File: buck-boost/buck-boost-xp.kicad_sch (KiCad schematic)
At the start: 0 parts

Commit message: Working on power stage of buck-boost plat
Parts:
- added C10, C11, C8, C9: TBD, Capacitor_THT:CP_Radial_D18.0mm_P7.50mm, symbol Device:C_Polarized
- added HS1: Q1, Heatsink:Heatsink_Stonecold_HS-132_32x14mm_2xFixation1.5mm, symbol Mechanical:Heatsink_Pad_2Pin
- added HS2: Q2, Heatsink:Heatsink_Stonecold_HS-132_32x14mm_2xFixation1.5mm, symbol Mechanical:Heatsink_Pad_2Pin
- added HS3: Q3, Heatsink:Heatsink_Stonecold_HS-132_32x14mm_2xFixation1.5mm, symbol Mechanical:Heatsink_Pad_2Pin
- added HS4: Q4, Heatsink:Heatsink_Stonecold_HS-132_32x14mm_2xFixation1.5mm, symbol Mechanical:Heatsink_Pad_2Pin
- added K1, K2: Relay_SPDT, symbol Relay:Relay_SPDT
- added L1: L_Small, symbol Device:L_Small
- added Q1, Q2, Q3, Q4: Q_NMOS_GDS, Package_TO_SOT_THT:TO-220-3_Vertical, symbol Device:Q_NMOS_GDS
- added R6: R_Small, symbol Device:R_Small
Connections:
- new net: L1.1, Q1.3 (S), Q2.2 (D)
- new net: K1.11, R6.1
- new net: C8.1, C9.1, K1.14, Q1.2 (D), R6.2
- new net: C10.1, C11.1, K2.14, Q3.2 (D)
- new net: C10.2, C11.2, Q4.3 (S)
- new net: C8.2, C9.2, Q2.3 (S)
- new net IL+: L1.2
- new net IL-: Q3.3 (S), Q4.2 (D)
- no-connect marks 0 -> 8
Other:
- note added: "Snubber?"

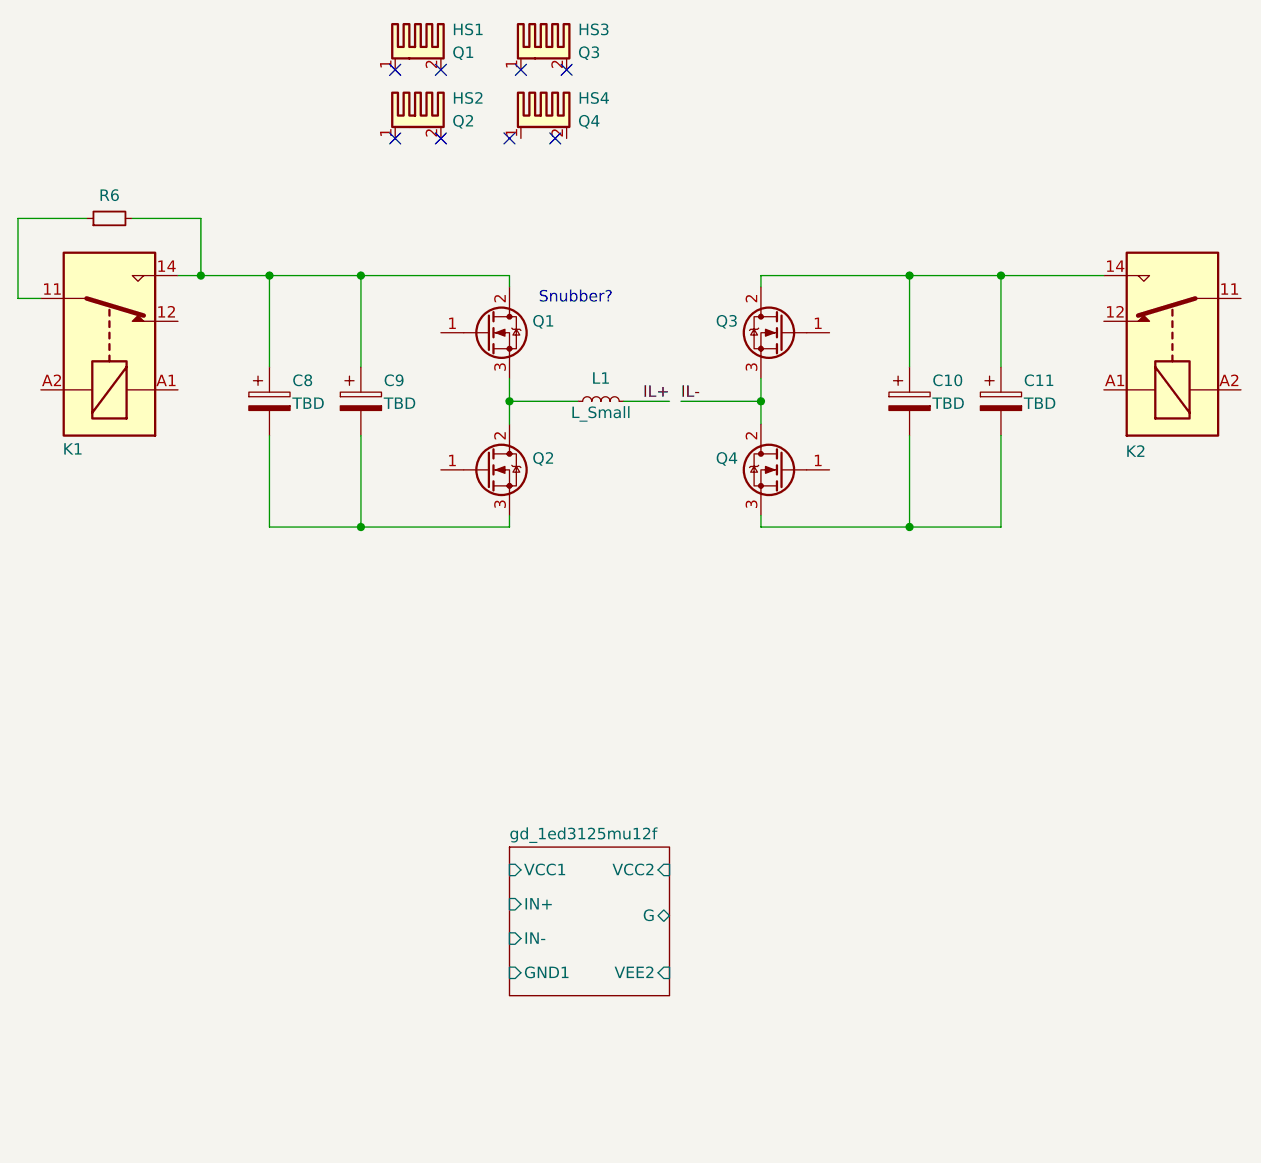
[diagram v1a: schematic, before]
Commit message: Schematics for power stage
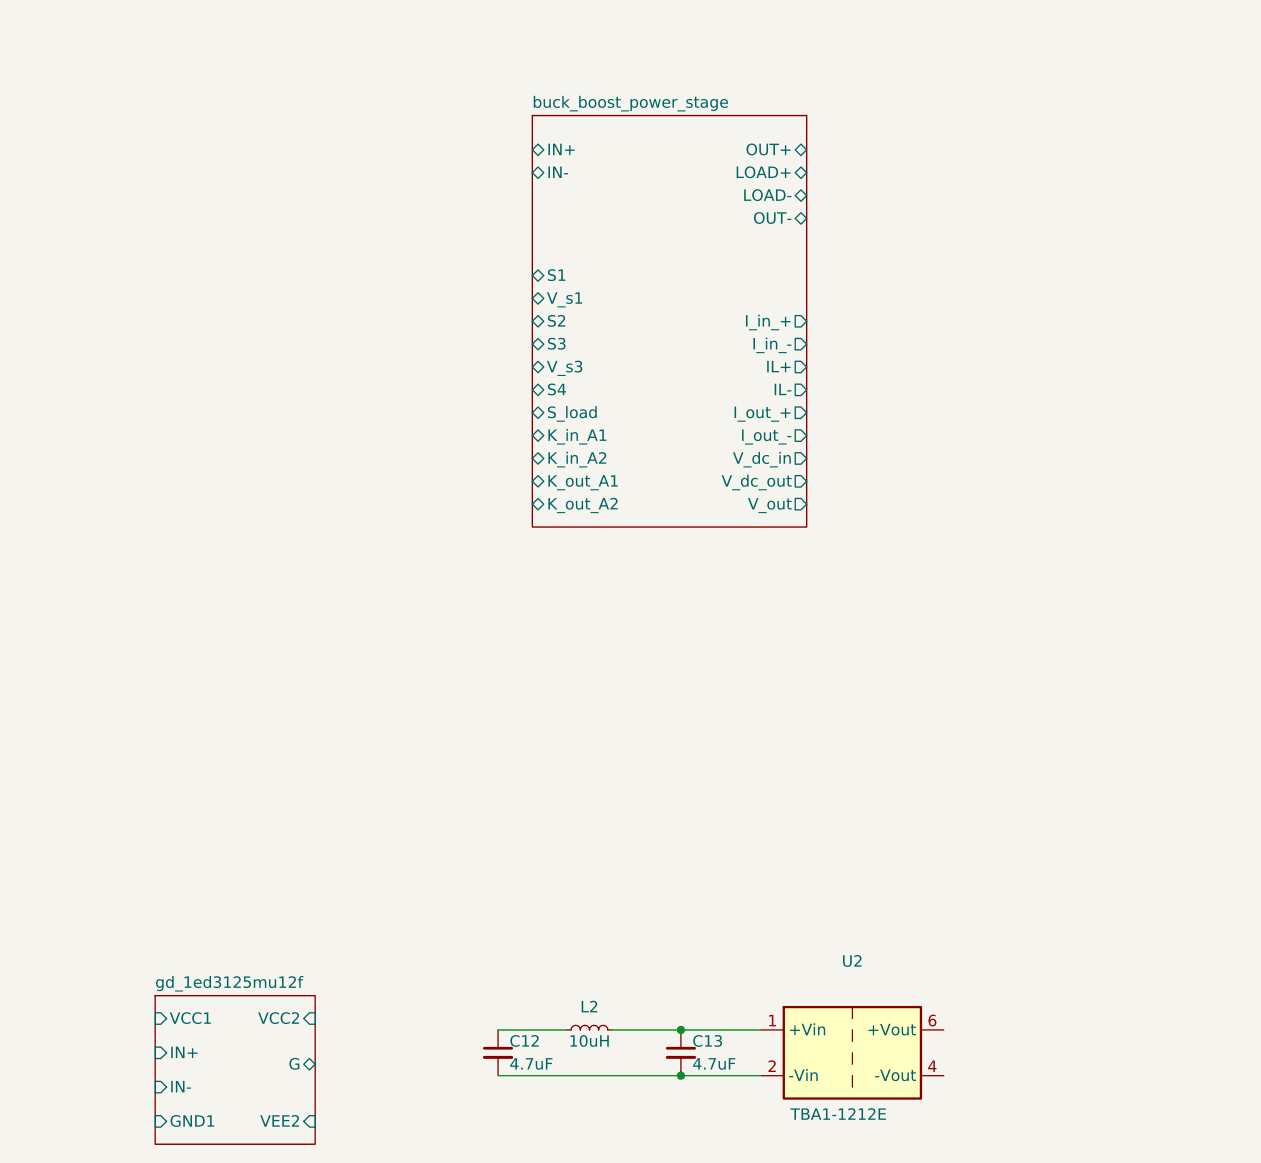
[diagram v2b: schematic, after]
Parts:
- removed C10, C11, C8, C9: TBD, Capacitor_THT:CP_Radial_D18.0mm_P7.50mm, symbol Device:C_Polarized
- removed HS1: Q1, Heatsink:Heatsink_Stonecold_HS-132_32x14mm_2xFixation1.5mm, symbol Mechanical:Heatsink_Pad_2Pin
- removed HS2: Q2, Heatsink:Heatsink_Stonecold_HS-132_32x14mm_2xFixation1.5mm, symbol Mechanical:Heatsink_Pad_2Pin
- removed HS3: Q3, Heatsink:Heatsink_Stonecold_HS-132_32x14mm_2xFixation1.5mm, symbol Mechanical:Heatsink_Pad_2Pin
- removed HS4: Q4, Heatsink:Heatsink_Stonecold_HS-132_32x14mm_2xFixation1.5mm, symbol Mechanical:Heatsink_Pad_2Pin
- removed K1, K2: Relay_SPDT, symbol Relay:Relay_SPDT
- removed L1: L_Small, symbol Device:L_Small
- removed Q1, Q2, Q3, Q4: Q_NMOS_GDS, Package_TO_SOT_THT:TO-220-3_Vertical, symbol Device:Q_NMOS_GDS
- removed R6: R_Small, symbol Device:R_Small
- added C12, C13: 4.7uF, Capacitor_SMD:C_0805_2012Metric_Pad1.18x1.45mm_HandSolder, symbol Device:C_Small
- added L2: 10uH, symbol Device:L_Small
- added U2: TBA1-1212E, Converter_DCDC:Converter_DCDC_TRACO_TBA1-xxxxE_Single_THT, symbol Converter_DCDC:TBA1-1212E
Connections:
- new net: C13.1, L2.2, U2.1 (+Vin)
- new net: C12.2, C13.2, U2.2 (-Vin)
- new net: C12.1, L2.1
- no-connect marks 8 -> 0
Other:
- added sheet buck_boost_power_stage (buck_boost_power_stage.kicad_sch)
- note removed: "Snubber?"

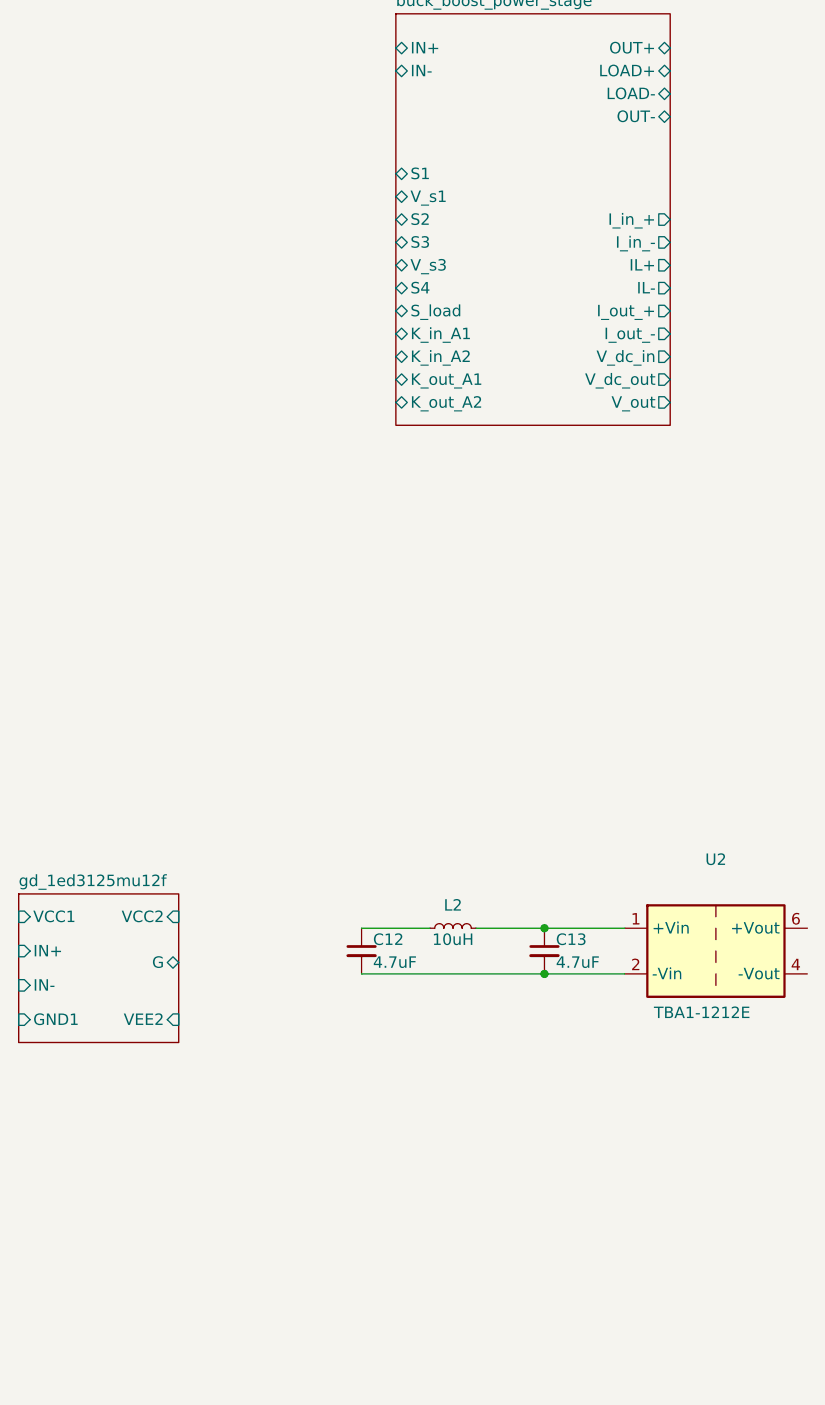
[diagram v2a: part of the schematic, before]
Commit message: Working on gate drivers of buck boost platform
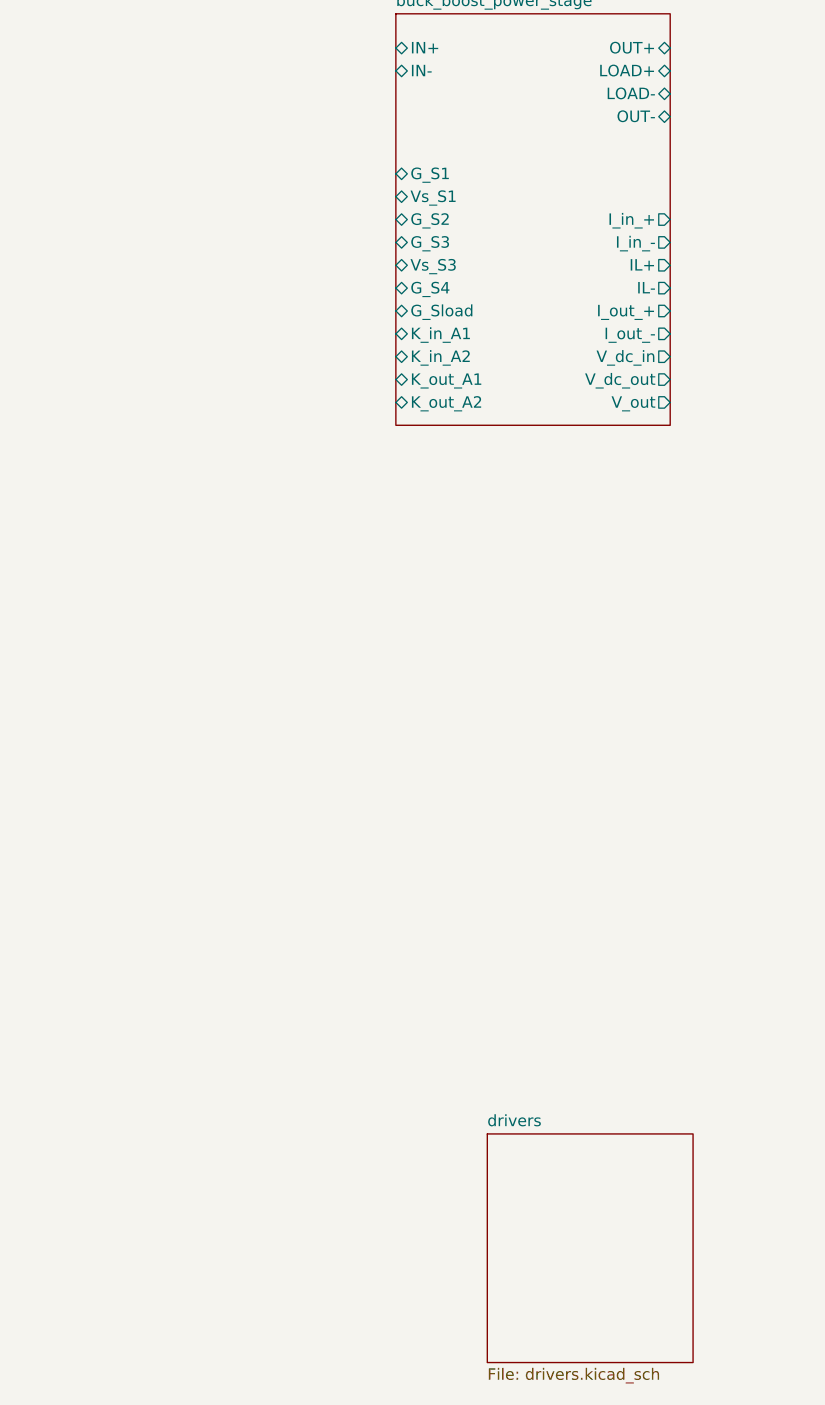
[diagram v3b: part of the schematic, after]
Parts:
- removed C12, C13: 4.7uF, Capacitor_SMD:C_0805_2012Metric_Pad1.18x1.45mm_HandSolder, symbol Device:C_Small
- removed L2: 10uH, symbol Device:L_Small
- removed U2: TBA1-1212E, Converter_DCDC:Converter_DCDC_TRACO_TBA1-xxxxE_Single_THT, symbol Converter_DCDC:TBA1-1212E
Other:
- removed sheet gd_1ed3125mu12f
- added sheet drivers (drivers.kicad_sch)
- sheet buck_boost_power_stage ports: added G_S1, G_S2, G_S3, G_S4, G_Sload, Vs_S1, Vs_S3; removed S1, S2, S3, S4, S_load, V_s1, V_s3

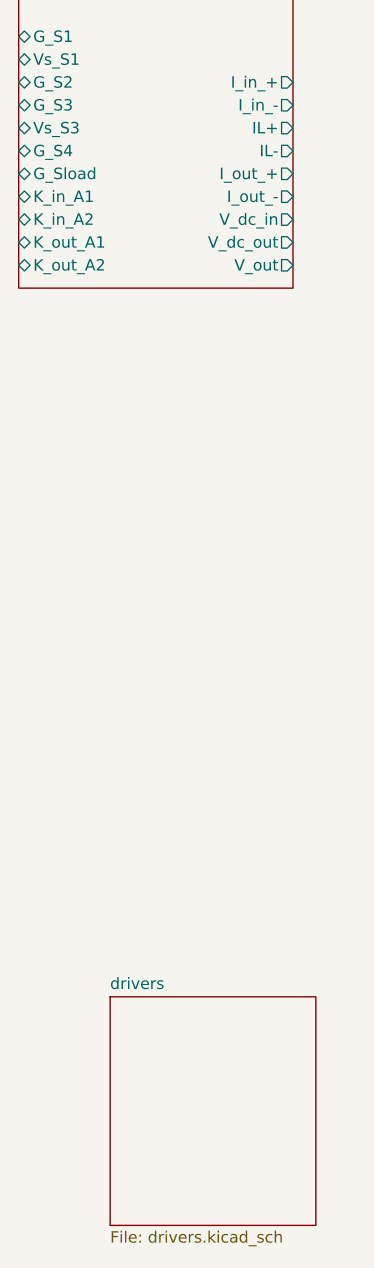
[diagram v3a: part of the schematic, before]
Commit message: Added load switch and relay drivers
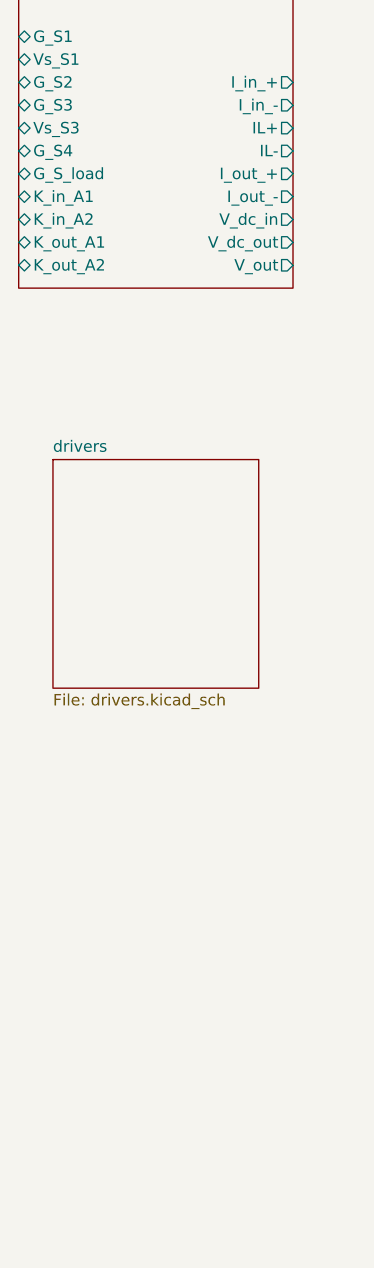
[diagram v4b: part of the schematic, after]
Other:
- sheet buck_boost_power_stage ports: added G_S_load; removed G_Sload
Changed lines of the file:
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@@
 			)
 		)
-		(pin "G_Sload" bidirectional
+		(pin "G_S_load" bidirectional
 			(at 85.09 58.42 180)
 			(effects
@@
 	)
 	(sheet
-		(at 95.25 149.86)
+		(at 88.9 90.17)
 		(size 22.86 25.4)
 		(fields_autoplaced yes)
@@
 		)
 		(property "Sheetname" "drivers"
-			(at 95.25 149.1484 0)
+			(at 88.9 89.4584 0)
 			(effects
 				(font
@@
 		)
 		(property "Sheetfile" "drivers.kicad_sch"
-			(at 95.25 175.8446 0)
+			(at 88.9 116.1546 0)
 			(effects
 				(font
